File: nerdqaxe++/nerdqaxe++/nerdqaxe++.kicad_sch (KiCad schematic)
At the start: 4 parts, among them J1 5.5mm/8A

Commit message: DFM
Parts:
- removed F1: 8A, myfootprints:fuseholder_littlefuse_blok, symbol Device:Fuse
- removed J1: 5.5mm/8A, qaxe:GCT_DCJ250-20-B-XX-X_REVA1, symbol mylib7:DCJ250-20
- added J1: XT30, qaxe:XT30PW-M, symbol bitaxe:XT30PW-M
- D1: Manufacturer SMBJ12A -> (none); PARTNO (none) -> SMBJ12A
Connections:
- net GND: now also J1.2 (GND)
- net Power/+12V: now also J1.1 (+V)
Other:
- sheet BM1366 renamed (lib_symbols 	(symbol "Device:C_Small" 		(pin_numbers 			(hide yes) 		) 		(pin_names 			(offset 0.254) 			(hide yes) 		) 		(exclude_from_sim no) 		(in_bom yes) 		(on_board yes) 		(property "Reference" "C" 			(at 0.254 1.778 0) 			(effects 				(font (size 1.27 1.27)) 				(justify left) 			) 		) 		(property "Value" "C_Small" 			(at 0.254 -2.032 0) 			(effects 				(font (size 1.27 1.27)) 				(justify left) 			) 		) 		(property "Footprint" "" 			(at 0 0 0) 			(effects 				(font (size 1.27 1.27)) 				(hide yes) 			) 		) 		(property "Datasheet" "~" 			(at 0 0 0) 			(effects 				(font (size 1.27 1.27)) 				(hide yes) 			) 		) 		(property "Description" "Unpolarized capacitor, small symbol" 			(at 0 0 0) 			(effects 				(font (size 1.27 1.27)) 				(hide yes) 			) 		) 		(property "ki_keywords" "capacitor cap" 			(at 0 0 0) 			(effects 				(font (size 1.27 1.27)) 				(hide yes) 			) 		) 		(property "ki_fp_filters" "C_*" 			(at 0 0 0) 			(effects 				(font (size 1.27 1.27)) 				(hide yes) 			) 		) 		(symbol "C_Small_0_1" 			(polyline 				(pts 					(xy -1.524 0.508) (xy 1.524 0.508) 				) 				(stroke (width 0.3048) (type default)) 				(fill (type none)) 			) 			(polyline 				(pts 					(xy -1.524 -0.508) (xy 1.524 -0.508) 				) 				(stroke (width 0.3302) (type default)) 				(fill (type none)) 			) 		) 		(symbol "C_Small_1_1" 			(pin passive line 				(at 0 2.54 270) 				(length 2.032) 				(name "~" 					(effects 						(font (size 1.27 1.27)) 					) 				) 				(number "1" 					(effects 						(font (size 1.27 1.27)) 					) 				) 			) 			(pin passive line 				(at 0 -2.54 90) 				(length 2.032) 				(name "~" 					(effects 						(font (size 1.27 1.27)) 					) 				) 				(number "2" 					(effects 						(font (size 1.27 1.27)) 					) 				) 			) 		) 		(embedded_fonts no) 	) ) (junction 	(at 226.06 66.04) 	(diameter 0) 	(color 0 0 0 0) 	(uuid "3484f984-c31f-4a34-8966-8e70daa440fd") ) (junction 	(at 243.84 74.93) 	(diameter 0) 	(color 0 0 0 0) 	(uuid "36952a2d-499b-49e1-afaa-586f493005a4") ) (junction 	(at 226.06 74.93) 	(diameter 0) 	(color 0 0 0 0) 	(uuid "4c954111-75e7-4069-8b6f-4b36027c61ae") ) (junction 	(at 243.84 66.04) 	(diameter 0) 	(color 0 0 0 0) 	(uuid "50c2631e-53b1-48fe-b313-db1e99abecf2") ) (junction 	(at 234.95 74.93) 	(diameter 0) 	(color 0 0 0 0) 	(uuid "58ca07ba-0178-4494-8d25-8357d06556ed") ) (junction 	(at 234.95 66.04) 	(diameter 0) 	(color 0 0 0 0) 	(uuid "84a034b5-3fd7-44ac-8b5d-c3bd155da8d8") ) (junction 	(at 217.17 66.04) 	(diameter 0) 	(color 0 0 0 0) 	(uuid "b19cc61e-6369-4c1d-9894-b7d7bf2a5037") ) (wire 	(pts 		(xy 234.95 66.04) (xy 226.06 66.04) 	) 	(stroke (width 0) (type default)) 	(uuid "0ffee5d9-b623-4f28-b426-e68799213a63") ) (wire 	(pts 		(xy 217.17 74.93) (xy 226.06 74.93) 	) 	(stroke (width 0) (type default)) 	(uuid "16e2d38d-13a1-460a-85ff-97e36fa0b454") ) (wire 	(pts 		(xy 226.06 66.04) (xy 217.17 66.04) 	) 	(stroke (width 0) (type default)) 	(uuid "19cf8b6b-1707-4229-b700-3f20dc5725be") ) (wire 	(pts 		(xy 226.06 66.04) (xy 226.06 67.31) 	) 	(stroke (width 0) (type default)) 	(uuid "1c77259d-206d-42ff-be1d-73fbc6801812") ) (wire 	(pts 		(xy 234.95 66.04) (xy 234.95 67.31) 	) 	(stroke (width 0) (type default)) 	(uuid "3e7fd837-d41a-4220-80f8-0693cda575c6") ) (wire 	(pts 		(xy 226.06 72.39) (xy 226.06 74.93) 	) 	(stroke (width 0) (type default)) 	(uuid "6f6bcfca-b4c3-47df-81da-9b375dff28a8") ) (wire 	(pts 		(xy 250.19 74.93) (xy 250.19 72.39) 	) 	(stroke (width 0) (type default)) 	(uuid "6f8e8e27-b1a6-4111-b226-c608b1c34840") ) (wire 	(pts 		(xy 217.17 66.04) (xy 217.17 67.31) 	) 	(stroke (width 0) (type default)) 	(uuid "93911aef-ca01-478c-9250-8fe5e7400ae9") ) (wire 	(pts 		(xy 243.84 74.93) (xy 250.19 74.93) 	) 	(stroke (width 0) (type default)) 	(uuid "a287f702-b4de-4751-80a5-188fdbbbe83d") ) (wire 	(pts 		(xy 243.84 66.04) (xy 243.84 67.31) 	) 	(stroke (width 0) (type default)) 	(uuid "a39641d6-f54e-46a3-9c37-a4245ca95139") ) (wire 	(pts 		(xy 250.19 66.04) (xy 243.84 66.04) 	) 	(stroke (width 0) (type default)) 	(uuid "ab98cdf3-e019-4195-bc3d-a52b85a73991") ) (wire 	(pts 		(xy 226.06 74.93) (xy 234.95 74.93) 	) 	(stroke (width 0) (type default)) 	(uuid "ad75b064-9ec6-4d78-bb4e-cc72d3c58237") ) (wire 	(pts 		(xy 234.95 74.93) (xy 243.84 74.93) 	) 	(stroke (width 0) (type default)) 	(uuid "afd5a4da-ff64-4e8d-b8a0-68dc8f59f9af") ) (wire 	(pts 		(xy 243.84 72.39) (xy 243.84 74.93) 	) 	(stroke (width 0) (type default)) 	(uuid "b3a8d4bd-3c9b-4de4-a5d2-e7c5ec35d2d0") ) (wire 	(pts 		(xy 234.95 72.39) (xy 234.95 74.93) 	) 	(stroke (width 0) (type default)) 	(uuid "bd78011e-6906-45b0-a009-9c454c1eba6a") ) (wire 	(pts 		(xy 250.19 67.31) (xy 250.19 66.04) 	) 	(stroke (width 0) (type default)) 	(uuid "d0f7bbde-0171-4ee7-8114-8afeeef317e0") ) (wire 	(pts 		(xy 217.17 66.04) (xy 205.74 66.04) 	) 	(stroke (width 0) (type default)) 	(uuid "f81f5721-42f5-45bb-94d8-c93378291771") ) (wire 	(pts 		(xy 217.17 72.39) (xy 217.17 74.93) 	) 	(stroke (width 0) (type default)) 	(uuid "f90526f4-a320-432c-9499-2c6d9a616a60") ) (wire 	(pts 		(xy 243.84 66.04) (xy 234.95 66.04) 	) 	(stroke (width 0) (type default)) 	(uuid "f9d31b11-9198-46b3-9d37-167425909b3e") ) (label "GND" 	(at 228.6 74.93 0) 	(effects 		(font (size 1.27 1.27)) 		(justify left bottom) 	) 	(uuid "15c04acc-f0ec-43c1-9bc3-7f66ee9d83a9") ) (symbol 	(lib_id "Device:C_Small") 	(at 217.17 69.85 0) 	(unit 1) 	(exclude_from_sim no) 	(in_bom yes) 	(on_board yes) 	(dnp no) 	(uuid "b18f5ac3-471a-45eb-a419-657532b2ea06") 	(property "Reference" "C58" 		(at 223.266 69.088 0) 		(effects 			(font (size 1.27 1.27)) 			(justify right) 		) 	) 	(property "Value" "10uF" 		(at 223.266 71.374 0) 		(effects 			(font (size 1.27 1.27)) 			(justify right) 		) 	) 	(property "Footprint" "Capacitor_SMD:C_0603_1608Metric" 		(at 217.17 69.85 0) 		(effects 			(font (size 1.27 1.27)) 			(hide yes) 		) 	) 	(property "Datasheet" "~" 		(at 217.17 69.85 0) 		(effects 			(font (size 1.27 1.27)) 			(hide yes) 		) 	) 	(property "Description" "Unpolarized capacitor, small symbol" 		(at 217.17 69.85 0) 		(effects 			(font (size 1.27 1.27)) 			(hide yes) 		) 	) 	(property "PARTNO" "GRM188R61E106KA73D" 		(at 217.17 69.85 0) 		(effects 			(font (size 1.27 1.27)) 			(hide yes) 		) 	) 	(property "DK" "490-18214-1-ND" 		(at 217.17 69.85 0) 		(effects 			(font (size 1.27 1.27)) 			(hide yes) 		) 	) 	(property "Voltage" "25V" 		(at 217.17 69.85 0) 		(effects 			(font (size 1.27 1.27)) 		) 	) 	(pin "1" 		(uuid "8af27835-538a-4c34-93c1-8cd8aa1e8183") 	) 	(pin "2" 		(uuid "cad85d99-dacf-4a66-8f17-46100b3887ee") 	) 	(instances 		(project "BitaxeGT" 			(path "" 				(reference "C58") 				(unit 1) 			) 		) 	) ) (symbol 	(lib_id "Device:C_Small") 	(at 250.19 69.85 0) 	(unit 1) 	(exclude_from_sim no) 	(in_bom yes) 	(on_board yes) 	(dnp no) 	(uuid "bfbb6926-e522-4a8e-aa67-ac2dbf6de58e") 	(property "Reference" "C62" 		(at 256.286 69.088 0) 		(effects 			(font (size 1.27 1.27)) 			(justify right) 		) 	) 	(property "Value" "10uF" 		(at 256.286 71.374 0) 		(effects 			(font (size 1.27 1.27)) 			(justify right) 		) 	) 	(property "Footprint" "Capacitor_SMD:C_0603_1608Metric" 		(at 250.19 69.85 0) 		(effects 			(font (size 1.27 1.27)) 			(hide yes) 		) 	) 	(property "Datasheet" "~" 		(at 250.19 69.85 0) 		(effects 			(font (size 1.27 1.27)) 			(hide yes) 		) 	) 	(property "Description" "Unpolarized capacitor, small symbol" 		(at 250.19 69.85 0) 		(effects 			(font (size 1.27 1.27)) 			(hide yes) 		) 	) 	(property "PARTNO" "GRM188R61E106KA73D" 		(at 250.19 69.85 0) 		(effects 			(font (size 1.27 1.27)) 			(hide yes) 		) 	) 	(property "DK" "490-18214-1-ND" 		(at 250.19 69.85 0) 		(effects 			(font (size 1.27 1.27)) 			(hide yes) 		) 	) 	(property "Voltage" "25V" 		(at 250.19 69.85 0) 		(effects 			(font (size 1.27 1.27)) 		) 	) 	(pin "1" 		(uuid "f7d25001-c0c9-44f2-898e-2c7e118423d5") 	) 	(pin "2" 		(uuid "de993016-33cd-4ff0-be0a-306482634e23") 	) 	(instances 		(project "BitaxeGT" 			(path "" 				(reference "C62") 				(unit 1) 			) 		) 	) ) (symbol 	(lib_id "Device:C_Small") 	(at 234.95 69.85 0) 	(unit 1) 	(exclude_from_sim no) 	(in_bom yes) 	(on_board yes) 	(dnp no) 	(uuid "0722fcdf-7845-48de-ba1d-ccf080e149ec") 	(property "Reference" "C60" 		(at 241.046 69.088 0) 		(effects 			(font (size 1.27 1.27)) 			(justify right) 		) 	) 	(property "Value" "10uF" 		(at 241.046 71.374 0) 		(effects 			(font (size 1.27 1.27)) 			(justify right) 		) 	) 	(property "Footprint" "Capacitor_SMD:C_0603_1608Metric" 		(at 234.95 69.85 0) 		(effects 			(font (size 1.27 1.27)) 			(hide yes) 		) 	) 	(property "Datasheet" "~" 		(at 234.95 69.85 0) 		(effects 			(font (size 1.27 1.27)) 			(hide yes) 		) 	) 	(property "Description" "Unpolarized capacitor, small symbol" 		(at 234.95 69.85 0) 		(effects 			(font (size 1.27 1.27)) 			(hide yes) 		) 	) 	(property "PARTNO" "GRM188R61E106KA73D" 		(at 234.95 69.85 0) 		(effects 			(font (size 1.27 1.27)) 			(hide yes) 		) 	) 	(property "DK" "490-18214-1-ND" 		(at 234.95 69.85 0) 		(effects 			(font (size 1.27 1.27)) 			(hide yes) 		) 	) 	(property "Voltage" "25V" 		(at 234.95 69.85 0) 		(effects 			(font (size 1.27 1.27)) 		) 	) 	(pin "1" 		(uuid "721fd6cb-8416-4974-8620-8fed067d83bc") 	) 	(pin "2" 		(uuid "d8e0a3c9-9e9e-41e3-bf0f-a336af67ec14") 	) 	(instances 		(project "BitaxeGT" 			(path "" 				(reference "C60") 				(unit 1) 			) 		) 	) ) (symbol 	(lib_id "Device:C_Small") 	(at 226.06 69.85 0) 	(unit 1) 	(exclude_from_sim no) 	(in_bom yes) 	(on_board yes) 	(dnp no) 	(uuid "2e47cf43-98b4-40c2-b0ea-c03ca27774ae") 	(property "Reference" "C59" 		(at 232.156 69.088 0) 		(effects 			(font (size 1.27 1.27)) 			(justify right) 		) 	) 	(property "Value" "10uF" 		(at 232.156 71.374 0) 		(effects 			(font (size 1.27 1.27)) 			(justify right) 		) 	) 	(property "Footprint" "Capacitor_SMD:C_0603_1608Metric" 		(at 226.06 69.85 0) 		(effects 			(font (size 1.27 1.27)) 			(hide yes) 		) 	) 	(property "Datasheet" "~" 		(at 226.06 69.85 0) 		(effects 			(font (size 1.27 1.27)) 			(hide yes) 		) 	) 	(property "Description" "Unpolarized capacitor, small symbol" 		(at 226.06 69.85 0) 		(effects 			(font (size 1.27 1.27)) 			(hide yes) 		) 	) 	(property "PARTNO" "GRM188R61E106KA73D" 		(at 226.06 69.85 0) 		(effects 			(font (size 1.27 1.27)) 			(hide yes) 		) 	) 	(property "DK" "490-18214-1-ND" 		(at 226.06 69.85 0) 		(effects 			(font (size 1.27 1.27)) 			(hide yes) 		) 	) 	(property "Voltage" "25V" 		(at 226.06 69.85 0) 		(effects 			(font (size 1.27 1.27)) 		) 	) 	(pin "1" 		(uuid "573eedd7-3011-4004-a97b-b59dad789d12") 	) 	(pin "2" 		(uuid "6fc83487-311d-4d7e-aa0b-6f9ebddee355") 	) 	(instances 		(project "BitaxeGT" 			(path "" 				(reference "C59") 				(unit 1) 			) 		) 	) ) (symbol 	(lib_id "Device:C_Small") 	(at 243.84 69.85 0) 	(unit 1) 	(exclude_from_sim no) 	(in_bom yes) 	(on_board yes) 	(dnp no) 	(uuid "74a02440-0509-4031-8135-c4e4af2eb67d") 	(property "Reference" "C61" 		(at 249.936 69.088 0) 		(effects 			(font (size 1.27 1.27)) 			(justify right) 		) 	) 	(property "Value" "10uF" 		(at 249.936 71.374 0) 		(effects 			(font (size 1.27 1.27)) 			(justify right) 		) 	) 	(property "Footprint" "Capacitor_SMD:C_0603_1608Metric" 		(at 243.84 69.85 0) 		(effects 			(font (size 1.27 1.27)) 			(hide yes) 		) 	) 	(property "Datasheet" "~" 		(at 243.84 69.85 0) 		(effects 			(font (size 1.27 1.27)) 			(hide yes) 		) 	) 	(property "Description" "Unpolarized capacitor, small symbol" 		(at 243.84 69.85 0) 		(effects 			(font (size 1.27 1.27)) 			(hide yes) 		) 	) 	(property "PARTNO" "GRM188R61E106KA73D" 		(at 243.84 69.85 0) 		(effects 			(font (size 1.27 1.27)) 			(hide yes) 		) 	) 	(property "DK" "490-18214-1-ND" 		(at 243.84 69.85 0) 		(effects 			(font (size 1.27 1.27)) 			(hide yes) 		) 	) 	(property "Voltage" "25V" 		(at 243.84 69.85 0) 		(effects 			(font (size 1.27 1.27)) 		) 	) 	(pin "1" 		(uuid "d2bf9b70-5e66-46ea-8409-c3d84d76877e") 	) 	(pin "2" 		(uuid "baf4bdcb-7117-473d-8c11-2664bee9a185") 	) 	(instances 		(project "BitaxeGT" 			(path "" 				(reference "C61") 				(unit 1) 			) 		) 	) )

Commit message: mounting holes
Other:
- sheet (lib_symbols 	(symbol "Device:C_Small" 		(pin_numbers 			(hide yes) 		) 		(pin_names 			(offset 0.254) 			(hide yes) 		) 		(exclude_from_sim no) 		(in_bom yes) 		(on_board yes) 		(property "Reference" "C" 			(at 0.254 1.778 0) 			(effects 				(font (size 1.27 1.27)) 				(justify left) 			) 		) 		(property "Value" "C_Small" 			(at 0.254 -2.032 0) 			(effects 				(font (size 1.27 1.27)) 				(justify left) 			) 		) 		(property "Footprint" "" 			(at 0 0 0) 			(effects 				(font (size 1.27 1.27)) 				(hide yes) 			) 		) 		(property "Datasheet" "~" 			(at 0 0 0) 			(effects 				(font (size 1.27 1.27)) 				(hide yes) 			) 		) 		(property "Description" "Unpolarized capacitor, small symbol" 			(at 0 0 0) 			(effects 				(font (size 1.27 1.27)) 				(hide yes) 			) 		) 		(property "ki_keywords" "capacitor cap" 			(at 0 0 0) 			(effects 				(font (size 1.27 1.27)) 				(hide yes) 			) 		) 		(property "ki_fp_filters" "C_*" 			(at 0 0 0) 			(effects 				(font (size 1.27 1.27)) 				(hide yes) 			) 		) 		(symbol "C_Small_0_1" 			(polyline 				(pts 					(xy -1.524 0.508) (xy 1.524 0.508) 				) 				(stroke (width 0.3048) (type default)) 				(fill (type none)) 			) 			(polyline 				(pts 					(xy -1.524 -0.508) (xy 1.524 -0.508) 				) 				(stroke (width 0.3302) (type default)) 				(fill (type none)) 			) 		) 		(symbol "C_Small_1_1" 			(pin passive line 				(at 0 2.54 270) 				(length 2.032) 				(name "~" 					(effects 						(font (size 1.27 1.27)) 					) 				) 				(number "1" 					(effects 						(font (size 1.27 1.27)) 					) 				) 			) 			(pin passive line 				(at 0 -2.54 90) 				(length 2.032) 				(name "~" 					(effects 						(font (size 1.27 1.27)) 					) 				) 				(number "2" 					(effects 						(font (size 1.27 1.27)) 					) 				) 			) 		) 		(embedded_fonts no) 	) ) (junction 	(at 226.06 66.04) 	(diameter 0) 	(color 0 0 0 0) 	(uuid "3484f984-c31f-4a34-8966-8e70daa440fd") ) (junction 	(at 243.84 74.93) 	(diameter 0) 	(color 0 0 0 0) 	(uuid "36952a2d-499b-49e1-afaa-586f493005a4") ) (junction 	(at 226.06 74.93) 	(diameter 0) 	(color 0 0 0 0) 	(uuid "4c954111-75e7-4069-8b6f-4b36027c61ae") ) (junction 	(at 243.84 66.04) 	(diameter 0) 	(color 0 0 0 0) 	(uuid "50c2631e-53b1-48fe-b313-db1e99abecf2") ) (junction 	(at 234.95 74.93) 	(diameter 0) 	(color 0 0 0 0) 	(uuid "58ca07ba-0178-4494-8d25-8357d06556ed") ) (junction 	(at 234.95 66.04) 	(diameter 0) 	(color 0 0 0 0) 	(uuid "84a034b5-3fd7-44ac-8b5d-c3bd155da8d8") ) (junction 	(at 217.17 66.04) 	(diameter 0) 	(color 0 0 0 0) 	(uuid "b19cc61e-6369-4c1d-9894-b7d7bf2a5037") ) (wire 	(pts 		(xy 234.95 66.04) (xy 226.06 66.04) 	) 	(stroke (width 0) (type default)) 	(uuid "0ffee5d9-b623-4f28-b426-e68799213a63") ) (wire 	(pts 		(xy 217.17 74.93) (xy 226.06 74.93) 	) 	(stroke (width 0) (type default)) 	(uuid "16e2d38d-13a1-460a-85ff-97e36fa0b454") ) (wire 	(pts 		(xy 226.06 66.04) (xy 217.17 66.04) 	) 	(stroke (width 0) (type default)) 	(uuid "19cf8b6b-1707-4229-b700-3f20dc5725be") ) (wire 	(pts 		(xy 226.06 66.04) (xy 226.06 67.31) 	) 	(stroke (width 0) (type default)) 	(uuid "1c77259d-206d-42ff-be1d-73fbc6801812") ) (wire 	(pts 		(xy 234.95 66.04) (xy 234.95 67.31) 	) 	(stroke (width 0) (type default)) 	(uuid "3e7fd837-d41a-4220-80f8-0693cda575c6") ) (wire 	(pts 		(xy 226.06 72.39) (xy 226.06 74.93) 	) 	(stroke (width 0) (type default)) 	(uuid "6f6bcfca-b4c3-47df-81da-9b375dff28a8") ) (wire 	(pts 		(xy 250.19 74.93) (xy 250.19 72.39) 	) 	(stroke (width 0) (type default)) 	(uuid "6f8e8e27-b1a6-4111-b226-c608b1c34840") ) (wire 	(pts 		(xy 217.17 66.04) (xy 217.17 67.31) 	) 	(stroke (width 0) (type default)) 	(uuid "93911aef-ca01-478c-9250-8fe5e7400ae9") ) (wire 	(pts 		(xy 243.84 74.93) (xy 250.19 74.93) 	) 	(stroke (width 0) (type default)) 	(uuid "a287f702-b4de-4751-80a5-188fdbbbe83d") ) (wire 	(pts 		(xy 243.84 66.04) (xy 243.84 67.31) 	) 	(stroke (width 0) (type default)) 	(uuid "a39641d6-f54e-46a3-9c37-a4245ca95139") ) (wire 	(pts 		(xy 250.19 66.04) (xy 243.84 66.04) 	) 	(stroke (width 0) (type default)) 	(uuid "ab98cdf3-e019-4195-bc3d-a52b85a73991") ) (wire 	(pts 		(xy 226.06 74.93) (xy 234.95 74.93) 	) 	(stroke (width 0) (type default)) 	(uuid "ad75b064-9ec6-4d78-bb4e-cc72d3c58237") ) (wire 	(pts 		(xy 234.95 74.93) (xy 243.84 74.93) 	) 	(stroke (width 0) (type default)) 	(uuid "afd5a4da-ff64-4e8d-b8a0-68dc8f59f9af") ) (wire 	(pts 		(xy 243.84 72.39) (xy 243.84 74.93) 	) 	(stroke (width 0) (type default)) 	(uuid "b3a8d4bd-3c9b-4de4-a5d2-e7c5ec35d2d0") ) (wire 	(pts 		(xy 234.95 72.39) (xy 234.95 74.93) 	) 	(stroke (width 0) (type default)) 	(uuid "bd78011e-6906-45b0-a009-9c454c1eba6a") ) (wire 	(pts 		(xy 250.19 67.31) (xy 250.19 66.04) 	) 	(stroke (width 0) (type default)) 	(uuid "d0f7bbde-0171-4ee7-8114-8afeeef317e0") ) (wire 	(pts 		(xy 217.17 66.04) (xy 205.74 66.04) 	) 	(stroke (width 0) (type default)) 	(uuid "f81f5721-42f5-45bb-94d8-c93378291771") ) (wire 	(pts 		(xy 217.17 72.39) (xy 217.17 74.93) 	) 	(stroke (width 0) (type default)) 	(uuid "f90526f4-a320-432c-9499-2c6d9a616a60") ) (wire 	(pts 		(xy 243.84 66.04) (xy 234.95 66.04) 	) 	(stroke (width 0) (type default)) 	(uuid "f9d31b11-9198-46b3-9d37-167425909b3e") ) (label "GND" 	(at 228.6 74.93 0) 	(effects 		(font (size 1.27 1.27)) 		(justify left bottom) 	) 	(uuid "15c04acc-f0ec-43c1-9bc3-7f66ee9d83a9") ) (symbol 	(lib_id "Device:C_Small") 	(at 217.17 69.85 0) 	(unit 1) 	(exclude_from_sim no) 	(in_bom yes) 	(on_board yes) 	(dnp no) 	(uuid "b18f5ac3-471a-45eb-a419-657532b2ea06") 	(property "Reference" "C58" 		(at 223.266 69.088 0) 		(effects 			(font (size 1.27 1.27)) 			(justify right) 		) 	) 	(property "Value" "10uF" 		(at 223.266 71.374 0) 		(effects 			(font (size 1.27 1.27)) 			(justify right) 		) 	) 	(property "Footprint" "Capacitor_SMD:C_0603_1608Metric" 		(at 217.17 69.85 0) 		(effects 			(font (size 1.27 1.27)) 			(hide yes) 		) 	) 	(property "Datasheet" "~" 		(at 217.17 69.85 0) 		(effects 			(font (size 1.27 1.27)) 			(hide yes) 		) 	) 	(property "Description" "Unpolarized capacitor, small symbol" 		(at 217.17 69.85 0) 		(effects 			(font (size 1.27 1.27)) 			(hide yes) 		) 	) 	(property "PARTNO" "GRM188R61E106KA73D" 		(at 217.17 69.85 0) 		(effects 			(font (size 1.27 1.27)) 			(hide yes) 		) 	) 	(property "DK" "490-18214-1-ND" 		(at 217.17 69.85 0) 		(effects 			(font (size 1.27 1.27)) 			(hide yes) 		) 	) 	(property "Voltage" "25V" 		(at 217.17 69.85 0) 		(effects 			(font (size 1.27 1.27)) 		) 	) 	(pin "1" 		(uuid "8af27835-538a-4c34-93c1-8cd8aa1e8183") 	) 	(pin "2" 		(uuid "cad85d99-dacf-4a66-8f17-46100b3887ee") 	) 	(instances 		(project "BitaxeGT" 			(path "" 				(reference "C58") 				(unit 1) 			) 		) 	) ) (symbol 	(lib_id "Device:C_Small") 	(at 250.19 69.85 0) 	(unit 1) 	(exclude_from_sim no) 	(in_bom yes) 	(on_board yes) 	(dnp no) 	(uuid "bfbb6926-e522-4a8e-aa67-ac2dbf6de58e") 	(property "Reference" "C62" 		(at 256.286 69.088 0) 		(effects 			(font (size 1.27 1.27)) 			(justify right) 		) 	) 	(property "Value" "10uF" 		(at 256.286 71.374 0) 		(effects 			(font (size 1.27 1.27)) 			(justify right) 		) 	) 	(property "Footprint" "Capacitor_SMD:C_0603_1608Metric" 		(at 250.19 69.85 0) 		(effects 			(font (size 1.27 1.27)) 			(hide yes) 		) 	) 	(property "Datasheet" "~" 		(at 250.19 69.85 0) 		(effects 			(font (size 1.27 1.27)) 			(hide yes) 		) 	) 	(property "Description" "Unpolarized capacitor, small symbol" 		(at 250.19 69.85 0) 		(effects 			(font (size 1.27 1.27)) 			(hide yes) 		) 	) 	(property "PARTNO" "GRM188R61E106KA73D" 		(at 250.19 69.85 0) 		(effects 			(font (size 1.27 1.27)) 			(hide yes) 		) 	) 	(property "DK" "490-18214-1-ND" 		(at 250.19 69.85 0) 		(effects 			(font (size 1.27 1.27)) 			(hide yes) 		) 	) 	(property "Voltage" "25V" 		(at 250.19 69.85 0) 		(effects 			(font (size 1.27 1.27)) 		) 	) 	(pin "1" 		(uuid "f7d25001-c0c9-44f2-898e-2c7e118423d5") 	) 	(pin "2" 		(uuid "de993016-33cd-4ff0-be0a-306482634e23") 	) 	(instances 		(project "BitaxeGT" 			(path "" 				(reference "C62") 				(unit 1) 			) 		) 	) ) (symbol 	(lib_id "Device:C_Small") 	(at 234.95 69.85 0) 	(unit 1) 	(exclude_from_sim no) 	(in_bom yes) 	(on_board yes) 	(dnp no) 	(uuid "0722fcdf-7845-48de-ba1d-ccf080e149ec") 	(property "Reference" "C60" 		(at 241.046 69.088 0) 		(effects 			(font (size 1.27 1.27)) 			(justify right) 		) 	) 	(property "Value" "10uF" 		(at 241.046 71.374 0) 		(effects 			(font (size 1.27 1.27)) 			(justify right) 		) 	) 	(property "Footprint" "Capacitor_SMD:C_0603_1608Metric" 		(at 234.95 69.85 0) 		(effects 			(font (size 1.27 1.27)) 			(hide yes) 		) 	) 	(property "Datasheet" "~" 		(at 234.95 69.85 0) 		(effects 			(font (size 1.27 1.27)) 			(hide yes) 		) 	) 	(property "Description" "Unpolarized capacitor, small symbol" 		(at 234.95 69.85 0) 		(effects 			(font (size 1.27 1.27)) 			(hide yes) 		) 	) 	(property "PARTNO" "GRM188R61E106KA73D" 		(at 234.95 69.85 0) 		(effects 			(font (size 1.27 1.27)) 			(hide yes) 		) 	) 	(property "DK" "490-18214-1-ND" 		(at 234.95 69.85 0) 		(effects 			(font (size 1.27 1.27)) 			(hide yes) 		) 	) 	(property "Voltage" "25V" 		(at 234.95 69.85 0) 		(effects 			(font (size 1.27 1.27)) 		) 	) 	(pin "1" 		(uuid "721fd6cb-8416-4974-8620-8fed067d83bc") 	) 	(pin "2" 		(uuid "d8e0a3c9-9e9e-41e3-bf0f-a336af67ec14") 	) 	(instances 		(project "BitaxeGT" 			(path "" 				(reference "C60") 				(unit 1) 			) 		) 	) ) (symbol 	(lib_id "Device:C_Small") 	(at 226.06 69.85 0) 	(unit 1) 	(exclude_from_sim no) 	(in_bom yes) 	(on_board yes) 	(dnp no) 	(uuid "2e47cf43-98b4-40c2-b0ea-c03ca27774ae") 	(property "Reference" "C59" 		(at 232.156 69.088 0) 		(effects 			(font (size 1.27 1.27)) 			(justify right) 		) 	) 	(property "Value" "10uF" 		(at 232.156 71.374 0) 		(effects 			(font (size 1.27 1.27)) 			(justify right) 		) 	) 	(property "Footprint" "Capacitor_SMD:C_0603_1608Metric" 		(at 226.06 69.85 0) 		(effects 			(font (size 1.27 1.27)) 			(hide yes) 		) 	) 	(property "Datasheet" "~" 		(at 226.06 69.85 0) 		(effects 			(font (size 1.27 1.27)) 			(hide yes) 		) 	) 	(property "Description" "Unpolarized capacitor, small symbol" 		(at 226.06 69.85 0) 		(effects 			(font (size 1.27 1.27)) 			(hide yes) 		) 	) 	(property "PARTNO" "GRM188R61E106KA73D" 		(at 226.06 69.85 0) 		(effects 			(font (size 1.27 1.27)) 			(hide yes) 		) 	) 	(property "DK" "490-18214-1-ND" 		(at 226.06 69.85 0) 		(effects 			(font (size 1.27 1.27)) 			(hide yes) 		) 	) 	(property "Voltage" "25V" 		(at 226.06 69.85 0) 		(effects 			(font (size 1.27 1.27)) 		) 	) 	(pin "1" 		(uuid "573eedd7-3011-4004-a97b-b59dad789d12") 	) 	(pin "2" 		(uuid "6fc83487-311d-4d7e-aa0b-6f9ebddee355") 	) 	(instances 		(project "BitaxeGT" 			(path "" 				(reference "C59") 				(unit 1) 			) 		) 	) ) (symbol 	(lib_id "Device:C_Small") 	(at 243.84 69.85 0) 	(unit 1) 	(exclude_from_sim no) 	(in_bom yes) 	(on_board yes) 	(dnp no) 	(uuid "74a02440-0509-4031-8135-c4e4af2eb67d") 	(property "Reference" "C61" 		(at 249.936 69.088 0) 		(effects 			(font (size 1.27 1.27)) 			(justify right) 		) 	) 	(property "Value" "10uF" 		(at 249.936 71.374 0) 		(effects 			(font (size 1.27 1.27)) 			(justify right) 		) 	) 	(property "Footprint" "Capacitor_SMD:C_0603_1608Metric" 		(at 243.84 69.85 0) 		(effects 			(font (size 1.27 1.27)) 			(hide yes) 		) 	) 	(property "Datasheet" "~" 		(at 243.84 69.85 0) 		(effects 			(font (size 1.27 1.27)) 			(hide yes) 		) 	) 	(property "Description" "Unpolarized capacitor, small symbol" 		(at 243.84 69.85 0) 		(effects 			(font (size 1.27 1.27)) 			(hide yes) 		) 	) 	(property "PARTNO" "GRM188R61E106KA73D" 		(at 243.84 69.85 0) 		(effects 			(font (size 1.27 1.27)) 			(hide yes) 		) 	) 	(property "DK" "490-18214-1-ND" 		(at 243.84 69.85 0) 		(effects 			(font (size 1.27 1.27)) 			(hide yes) 		) 	) 	(property "Voltage" "25V" 		(at 243.84 69.85 0) 		(effects 			(font (size 1.27 1.27)) 		) 	) 	(pin "1" 		(uuid "d2bf9b70-5e66-46ea-8409-c3d84d76877e") 	) 	(pin "2" 		(uuid "baf4bdcb-7117-473d-8c11-2664bee9a185") 	) 	(instances 		(project "BitaxeGT" 			(path "" 				(reference "C61") 				(unit 1) 			) 		) 	) ) renamed BM1366
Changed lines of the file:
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@@
 			(color 255 255 194 1.0000)
+		)
+		(property "Sheetname" "BM1366"
+			(at 82.55 90.7284 0)
+			(effects
+				(font
+					(size 1.27 1.27)
+				)
+				(justify left bottom)
+			)
 		)
 		(property "Sheetfile" "bm1366.kicad_sch"

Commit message: VDD improvements
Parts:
- added H1, H2, H3, H4, H5, H6: MountingHole_Pad, qaxe:MountingHole_3.2mm_M3_Pad_Via, symbol Mechanical:MountingHole_Pad
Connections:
- net GND: now also H1.1, H2.1, H3.1, H4.1, H5.1, H6.1

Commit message: finishing up
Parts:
- D1: LCSC (none) -> C3001973; Manufacturer  (none) -> UMW(Youtai Semiconductor Co., Ltd.)
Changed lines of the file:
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@@
+			)
+		)
+		(property "Manufacturer " ""
+			(at 120.65 151.13 0)
+			(effects
+				(font
+					(size 1.27 1.27)
+				)
 			)
 		)
@@
 			)
 		)
+		(property "Manufacturer " ""
+			(at 92.71 151.13 0)
+			(effects
+				(font
+					(size 1.27 1.27)
+				)
+			)
+		)
 		(pin "1"
 		)
@@
 			)
 		)
+		(property "Manufacturer " ""
+			(at 25.4 53.34 0)
+			(effects
+				(font
+					(size 1.27 1.27)
+				)
+			)
+		)
 		(pin "3"
 		)
@@
 			)
 		)
+		(property "Manufacturer " ""
+			(at 43.18 151.13 0)
+			(effects
+				(font
+					(size 1.27 1.27)
+				)
+			)
+		)
 		(pin "1"
 		)
@@
 			)
 		)
+		(property "Manufacturer " ""
+			(at 110.49 151.13 0)
+			(effects
+				(font
+					(size 1.27 1.27)
+				)
+			)
+		)
 		(pin "1"
 		)
@@
 		)
 		(property "PARTNO" "SMBJ12A"
+			(at 55.245 58.42 0)
+			(effects
+				(font
+					(size 1.27 1.27)
+				)
+			)
+		)
+		(property "Manufacturer " "UMW(Youtai Semiconductor Co., Ltd.)"
+			(at 55.245 58.42 0)
+			(effects
+				(font
+					(size 1.27 1.27)
+				)
+			)
+		)
+		(property "LCSC" "C3001973"
 			(at 55.245 58.42 0)
 			(effects
@@
 			)
 		)
+		(property "Manufacturer " ""
+			(at 57.15 151.13 0)
+			(effects
+				(font
+					(size 1.27 1.27)
+				)
+			)
+		)
 		(pin "1"
 		)
@@
 			)
 		)
+		(property "Manufacturer " ""
+			(at 77.47 151.13 0)
+			(effects
+				(font
+					(size 1.27 1.27)
+				)
+			)
+		)
 		(pin "1"
 		)
@@
 			)
 		)
+		(property "Manufacturer " ""
+			(at 85.09 184.15 0)
+			(effects
+				(font
+					(size 1.27 1.27)
+				)
+			)
+		)

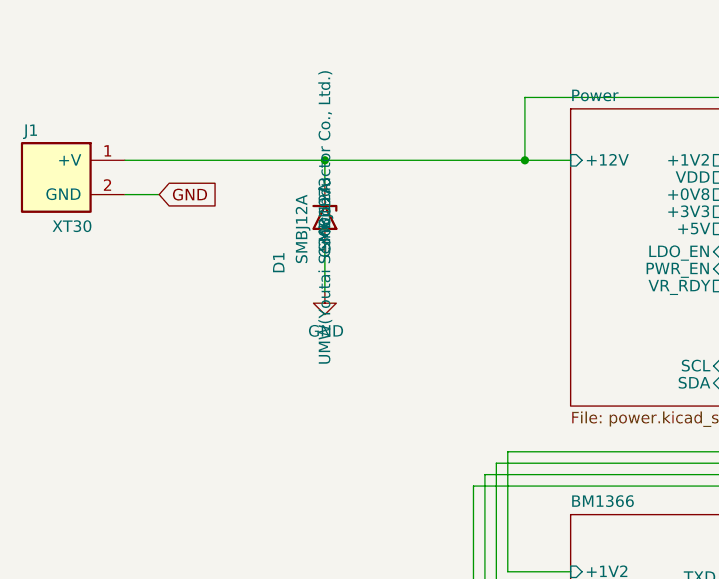
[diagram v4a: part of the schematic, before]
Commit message: hide unnecessary fields in schematic
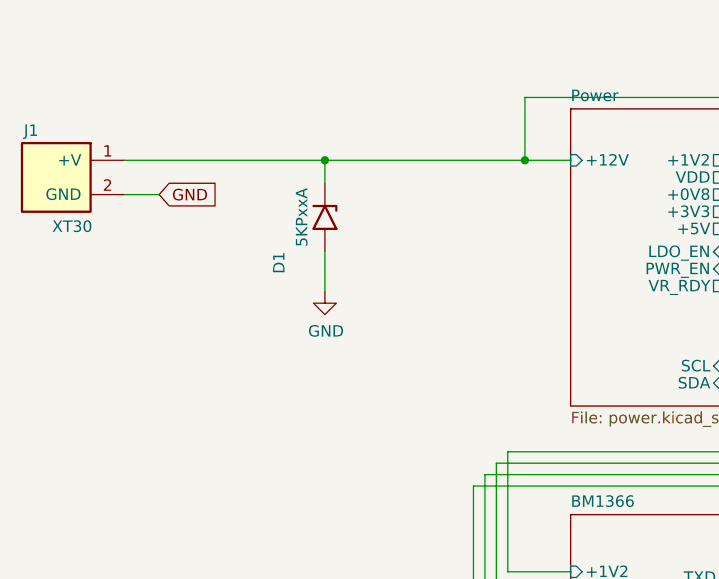
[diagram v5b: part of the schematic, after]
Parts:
- D1: value SMBJ12A -> 5KPxxA; footprint Diode_SMD:D_SMB -> Diode_THT:D_P600_R-6_P20.00mm_Horizontal
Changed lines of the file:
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@@
 					(size 1.27 1.27)
 				)
+				(hide yes)
 			)
 		)
@@
 					(size 1.27 1.27)
 				)
+				(hide yes)
 			)
 		)
@@
 					(size 1.27 1.27)
 				)
+				(hide yes)
 			)
 		)
@@
 					(size 1.27 1.27)
 				)
+				(hide yes)
 			)
 		)
@@
 					(size 1.27 1.27)
 				)
+				(hide yes)
 			)
 		)
@@
 			)
 		)
-		(property "Value" "SMBJ12A"
-			(at 52.705 55.88 0)
-			(effects
-				(font
-					(size 1.27 1.27)
-				)
-				(justify left)
-			)
-		)
-		(property "Footprint" "Diode_SMD:D_SMB"
+		(property "Value" "5KPxxA"
+			(at 52.705 58.42 0)
+			(effects
+				(font
+					(size 1.27 1.27)
+				)
+			)
+		)
+		(property "Footprint" "Diode_THT:D_P600_R-6_P20.00mm_Horizontal"
 			(at 50.165 58.42 0)
 			(effects
@@
 			)
 		)
-		(property "Datasheet" ""
+		(property "Datasheet" "https://diotec.com/tl_files/diotec/files/pdf/datasheets/5kp65.pdf"
 			(at 55.245 57.15 0)
 			(effects
@@
 			)
 		)
-		(property "Description" ""
+		(property "Description" "5000W unidirectional Transient Voltage Suppressor, P-600"
 			(at 55.245 58.42 0)
 			(effects
@@
 					(size 1.27 1.27)
 				)
+				(hide yes)
 			)
 		)
@@
 					(size 1.27 1.27)
 				)
+				(hide yes)
 			)
 		)
@@
 					(size 1.27 1.27)
 				)
+				(hide yes)
 			)
 		)
@@
 					(size 1.27 1.27)
 				)
+				(hide yes)
 			)
 		)
@@
 					(size 1.27 1.27)
 				)
+				(hide yes)
 			)
 		)
@@
 					(size 1.27 1.27)
 				)
-			)
-		)
+				(hide yes)
+			)
+		)

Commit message: schematic values cleanup
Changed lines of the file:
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@@
 		(dnp no)
 		(property "Reference" "D1"
-			(at 50.165 62.23 0)
+			(at 52.324 57.15 0)
 			(effects
 				(font
@@
 		)
 		(property "Value" "5KPxxA"
-			(at 52.705 58.42 0)
+			(at 58.166 58.42 0)
 			(effects
 				(font

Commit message: layout
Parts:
- D1: footprint Diode_THT:D_P600_R-6_P20.00mm_Horizontal -> Diode_SMD:D_SMB
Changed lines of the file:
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@@
 				)
 				(justify left)
+				(hide yes)
 			)
 		)
@@
 				)
 				(justify left)
+				(hide yes)
 			)
 		)
@@
 					(size 1.27 1.27)
 				)
+				(hide yes)
 			)
 		)
@@
 				)
 				(justify left)
+				(hide yes)
 			)
 		)
@@
 				)
 				(justify left)
+				(hide yes)
 			)
 		)
@@
 				)
 				(justify left)
+				(hide yes)
 			)
 		)
@@
 			)
 		)
-		(property "Footprint" "Diode_THT:D_P600_R-6_P20.00mm_Horizontal"
+		(property "Footprint" "Diode_SMD:D_SMB"
 			(at 50.165 58.42 0)
 			(effects
@@
 				)
 				(justify left)
+				(hide yes)
 			)
 		)
@@
 				)
 				(justify left)
+				(hide yes)
 			)
 		)
@@
 					(size 1.27 1.27)
 				)
-			)
-		)
+				(hide yes)
+			)
+		)

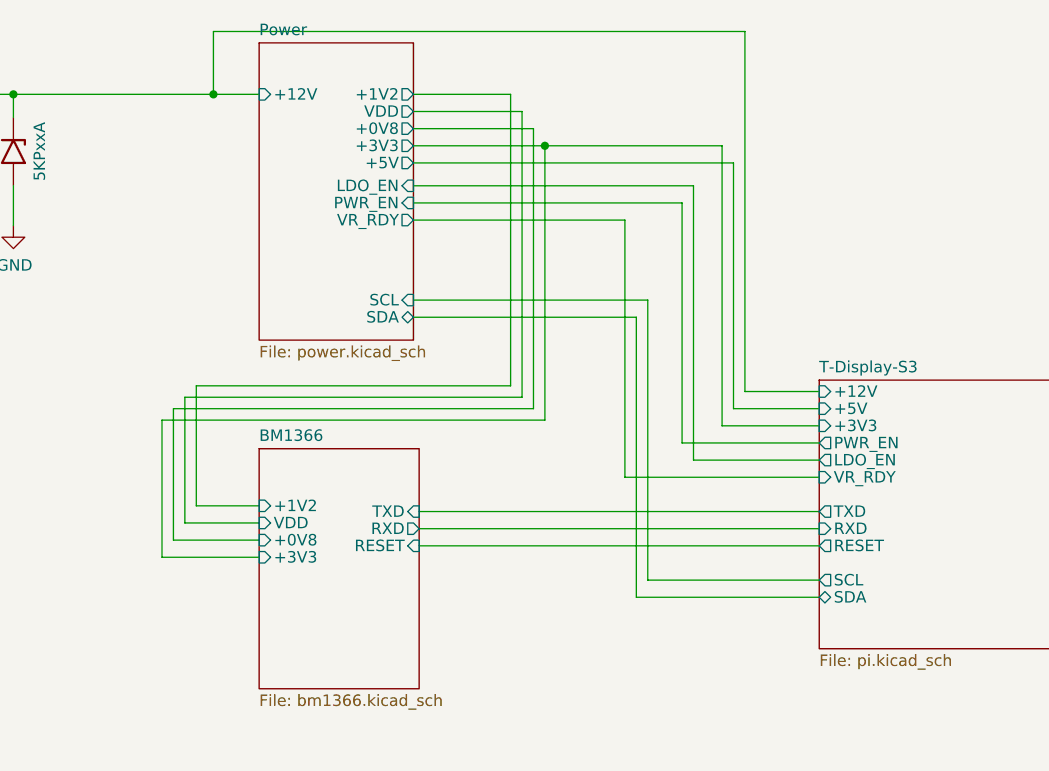
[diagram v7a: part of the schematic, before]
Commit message: clean DRC (incomplete)
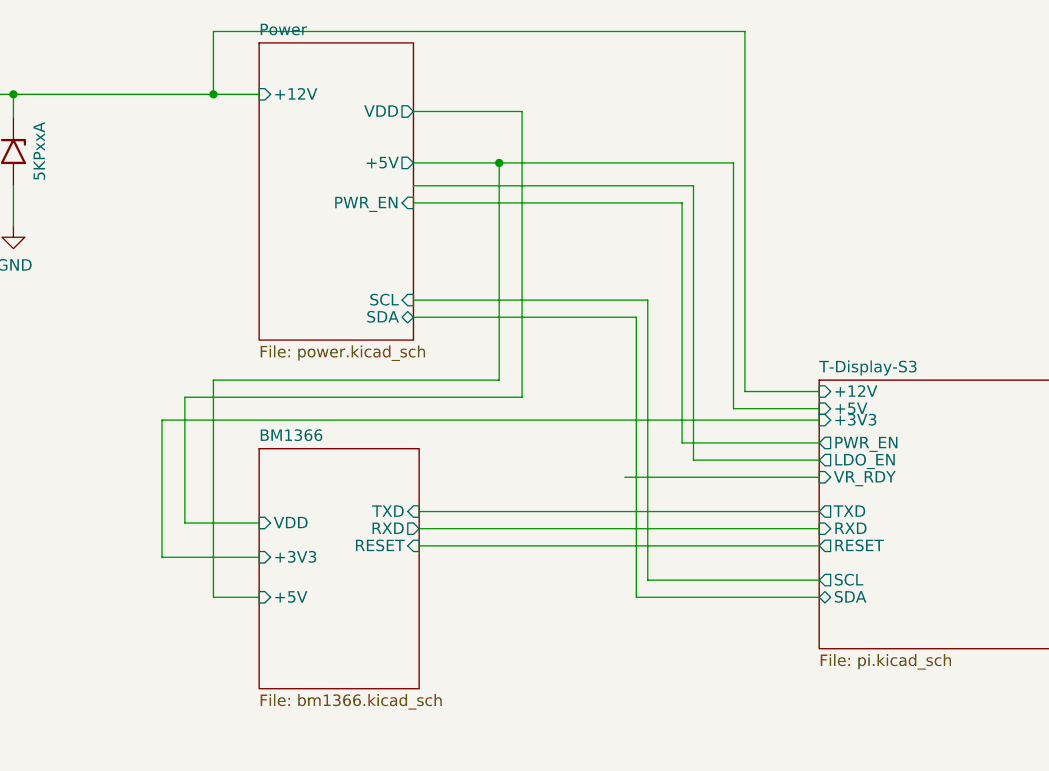
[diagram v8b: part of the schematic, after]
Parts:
- U1: value ~ -> (none)
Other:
- sheet BM1366 ports: added +5V; removed +0V8, +1V2
- sheet Power ports: added none; removed +0V8, +1V2, +3V3, LDO_EN, VR_RDY
